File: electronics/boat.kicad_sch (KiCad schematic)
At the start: 20 parts, among them J1 LeftESC, J2 UART1, J3 RightESC, M1 SG90 9g Micro Servo, M5 SG90 9g Micro Servo, M9 WaterPump_DC_DelavanAgPumpsDi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, Q1 IRLB3036/IRLZ34N, SW1 Reset, U1 XBee_SMT, U2 PIC32MX170F256B

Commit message: rearrange schematic
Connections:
- net +3V3: now also C8.1, R4.2, R5.1, SW1.1; no longer R5.2
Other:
- moved on the sheet: AE1, C5, C6, C7, C8, D2, J1, J2, J3, M1, M5, M9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

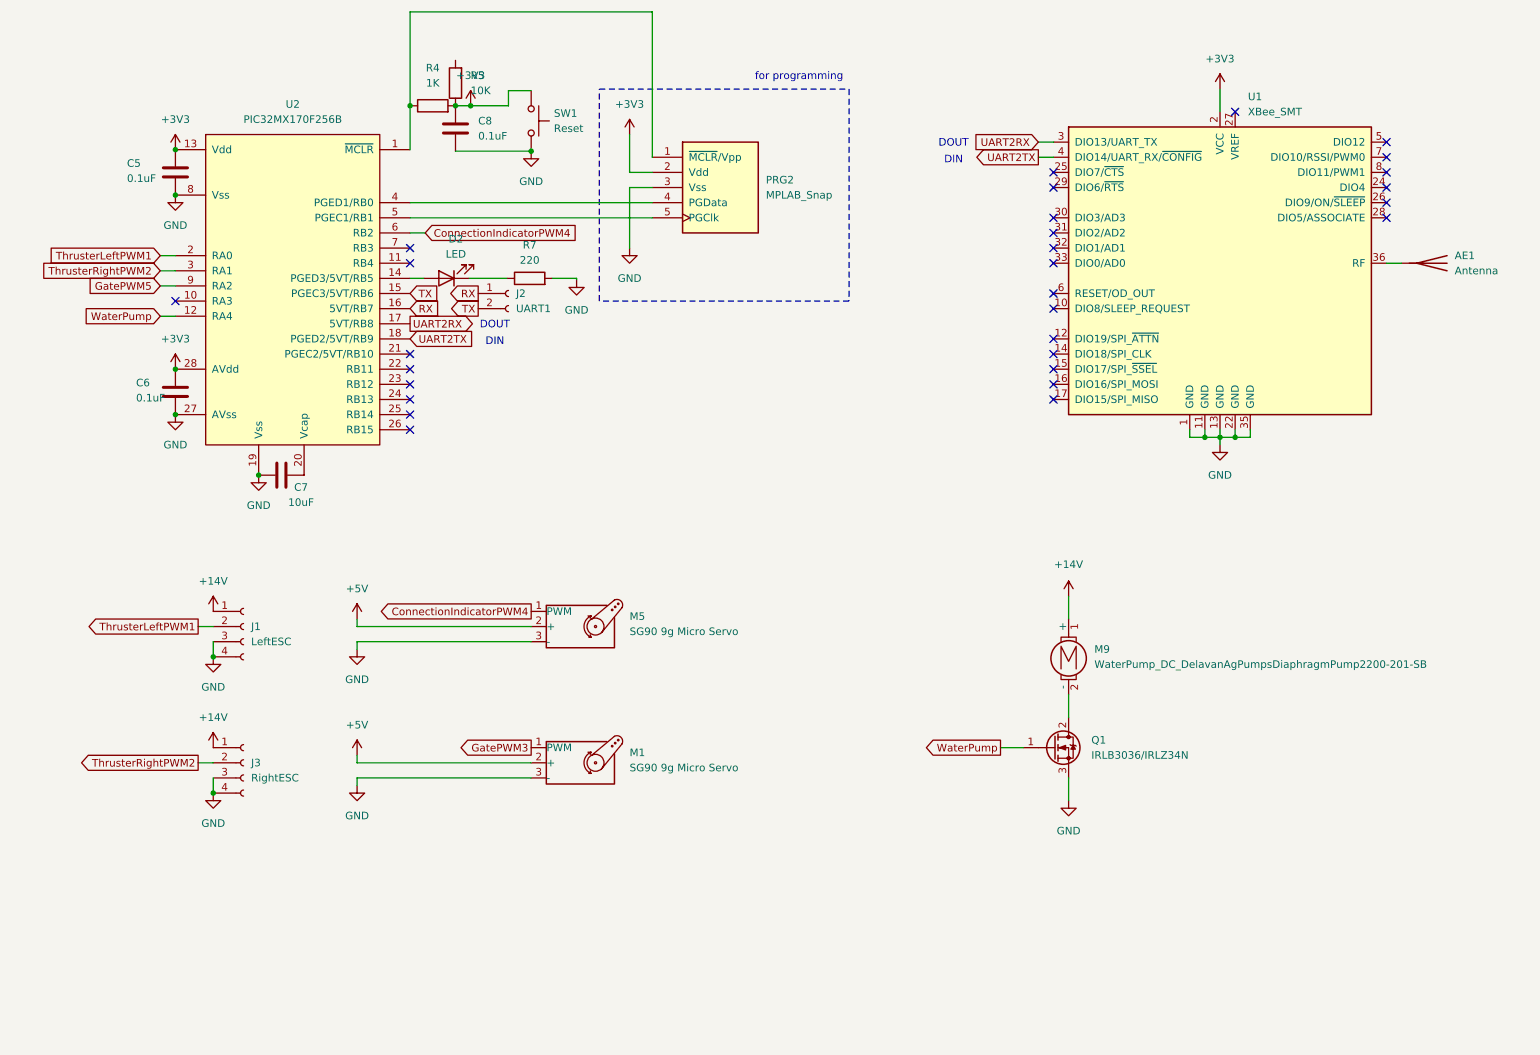
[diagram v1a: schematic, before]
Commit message: update and reorganize electronics for documentation
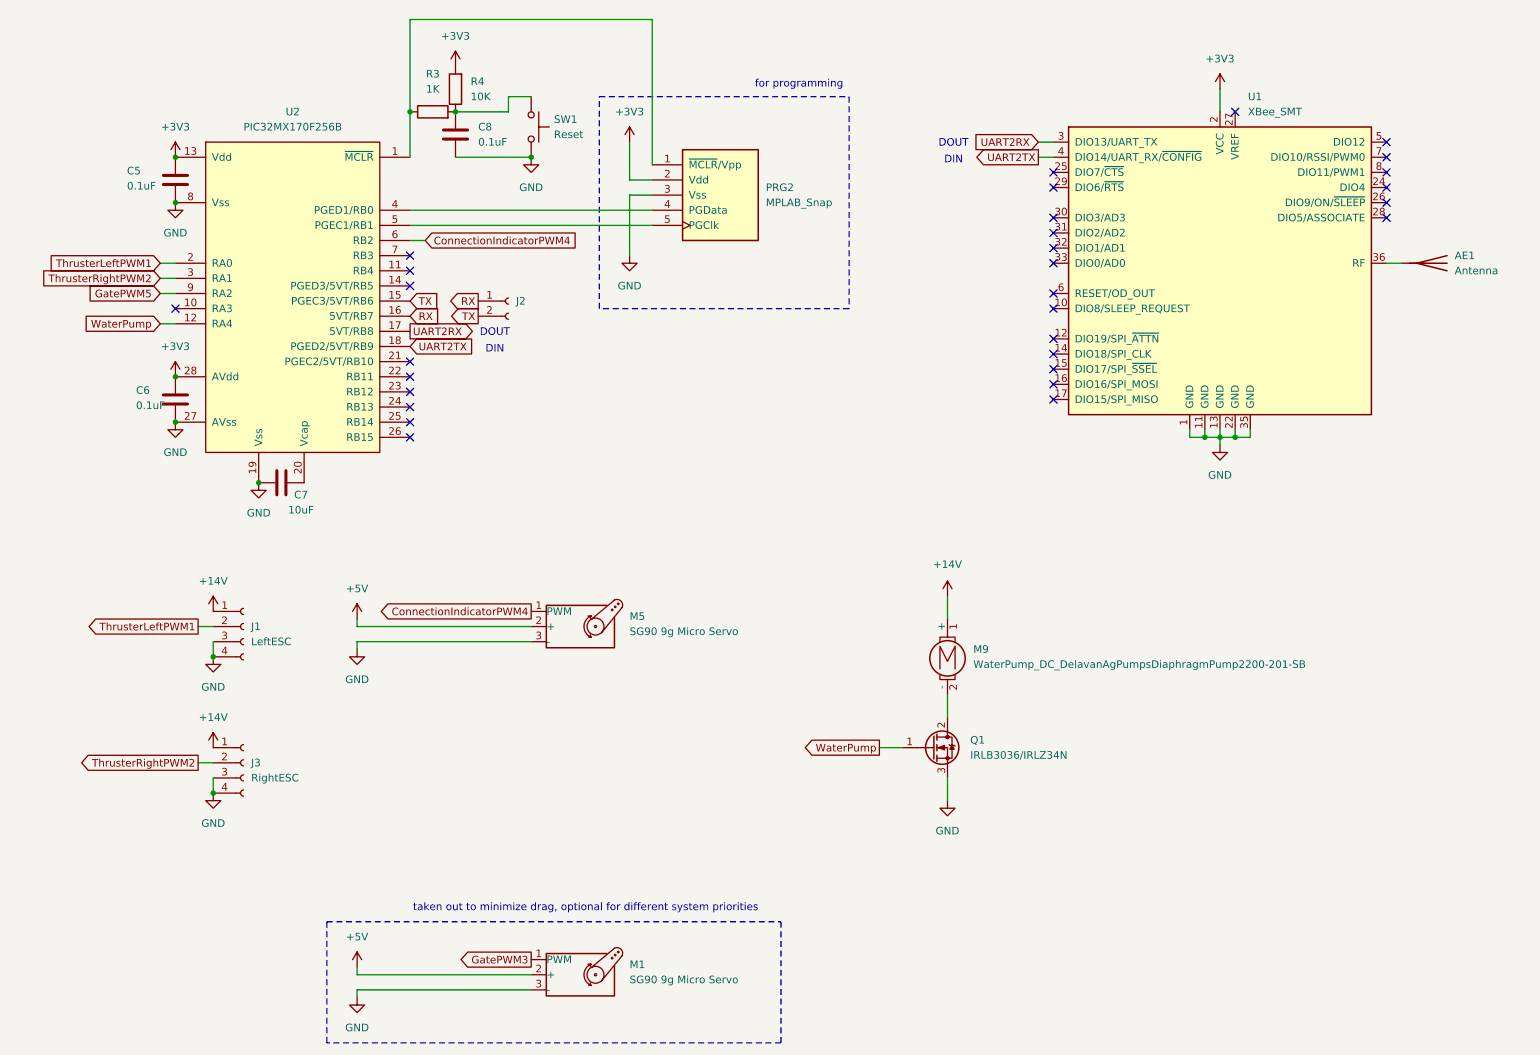
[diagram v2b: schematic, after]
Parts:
- removed D2: LED, symbol Device:LED
- removed R5: 10K, symbol ME218_BaseLib:Res2
- removed R7: 220, symbol Device:R
- added R3: 1K, symbol ME218_BaseLib:Res2
- R4: value 1K -> 10K
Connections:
- net +3V3: no longer C8.1, SW1.1
- net at PRG2.1 (~{MCLR}/Vpp), U2.1 (~{MCLR}): now also R3.1; no longer R4.1
- new net: C8.1, R3.2, R4.1, SW1.1
- no-connect marks 29 -> 30
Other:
- note added: "taken out to minimize drag, optional for different system priorities"
- moved on the sheet: C5, C6, C7, J2, M1, M9, PRG2, Q1, U2
